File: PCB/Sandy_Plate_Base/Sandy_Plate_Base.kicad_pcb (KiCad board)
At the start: 2 copper layers, 302.4 x 93 mm, 1 part

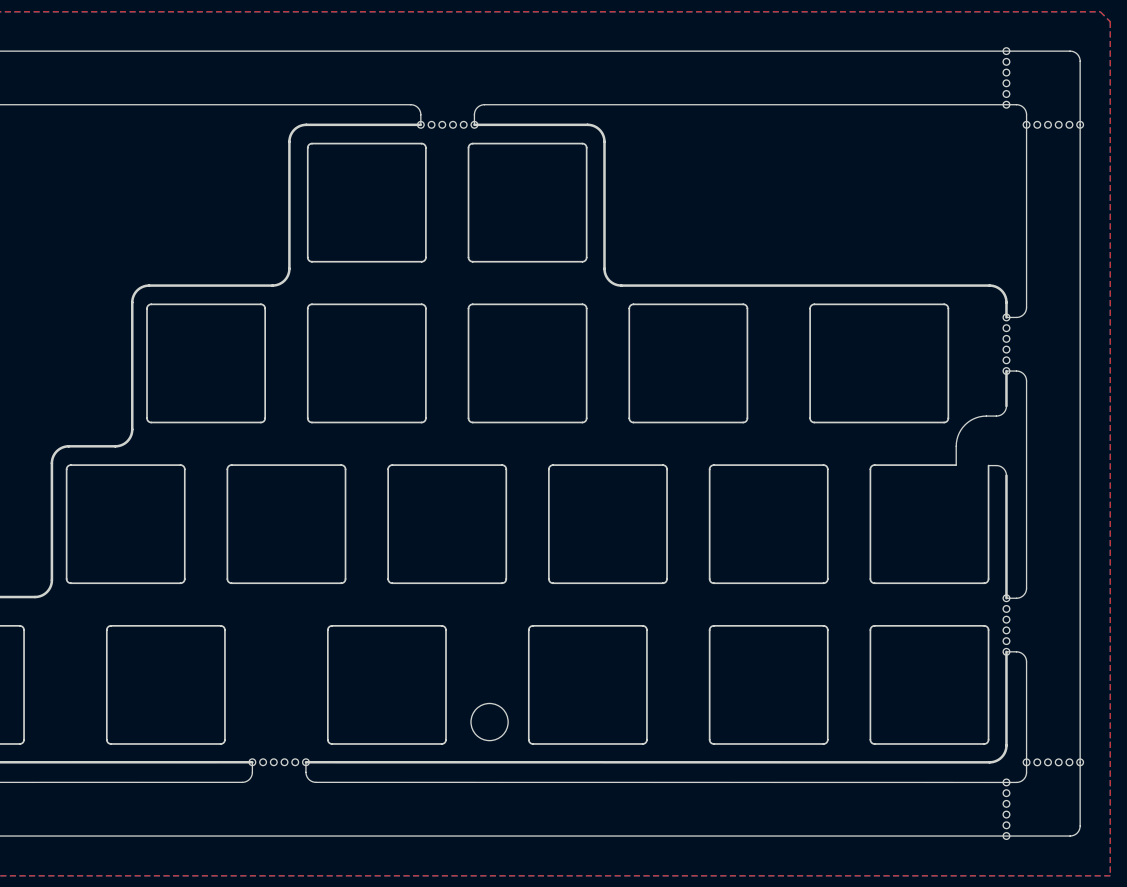
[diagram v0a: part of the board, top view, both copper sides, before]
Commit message: 製作したリビジョンを知りたいので、バージョン表記からリビジョン番号による表記へ変更
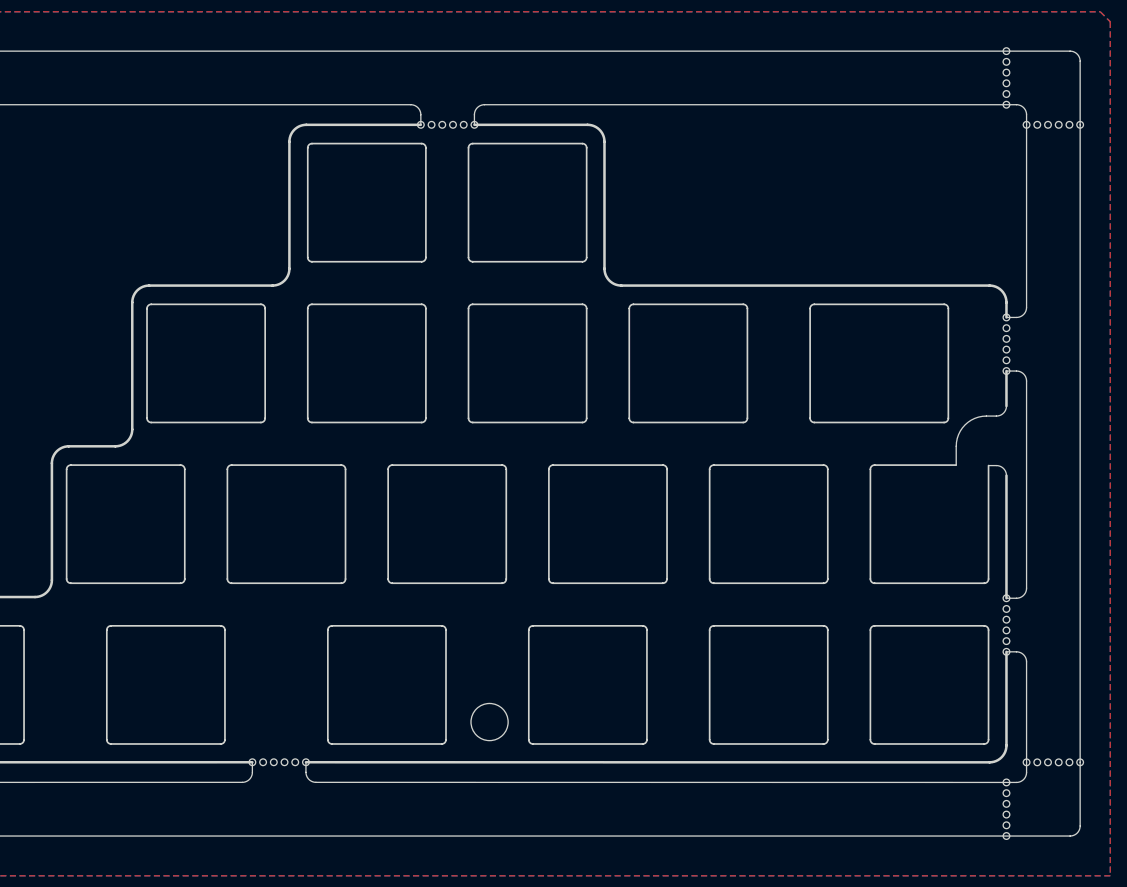
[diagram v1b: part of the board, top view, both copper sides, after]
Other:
- board text added: "#Sandy_kbd DN0020, Plate for Base by @jpskenn"
- board text removed: "#Sandy_kbd v.0.2, Plate for Base by @jpskenn"

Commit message: 改善：基板うら側を示すシルクを目立つように変更
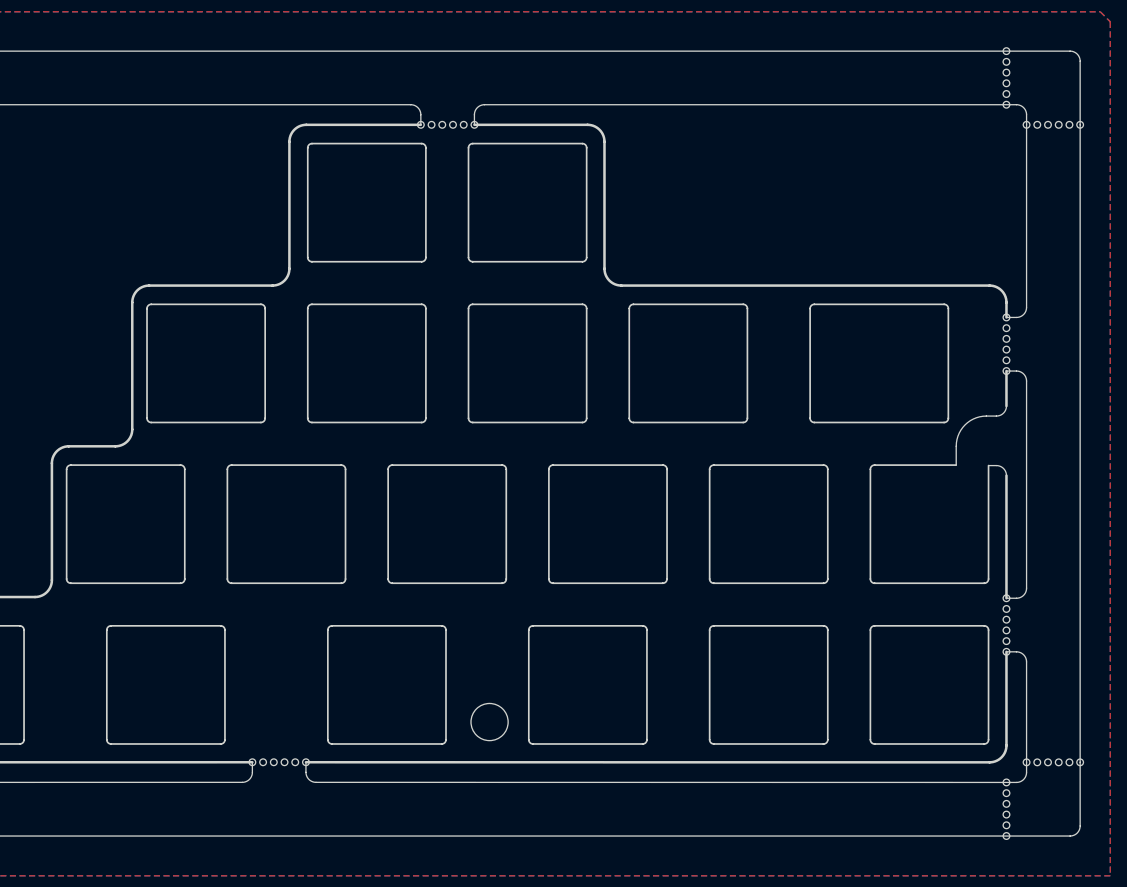
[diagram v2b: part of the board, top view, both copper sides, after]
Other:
- board text added: "Back Side"
